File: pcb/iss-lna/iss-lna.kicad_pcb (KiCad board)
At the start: 2 copper layers, 65 x 32 mm, 46 parts, among them J1 SMA, J2 UFL, J3 UFL, J4 SMA, J5 UFL, J6 UFL, Q1 BFU520R

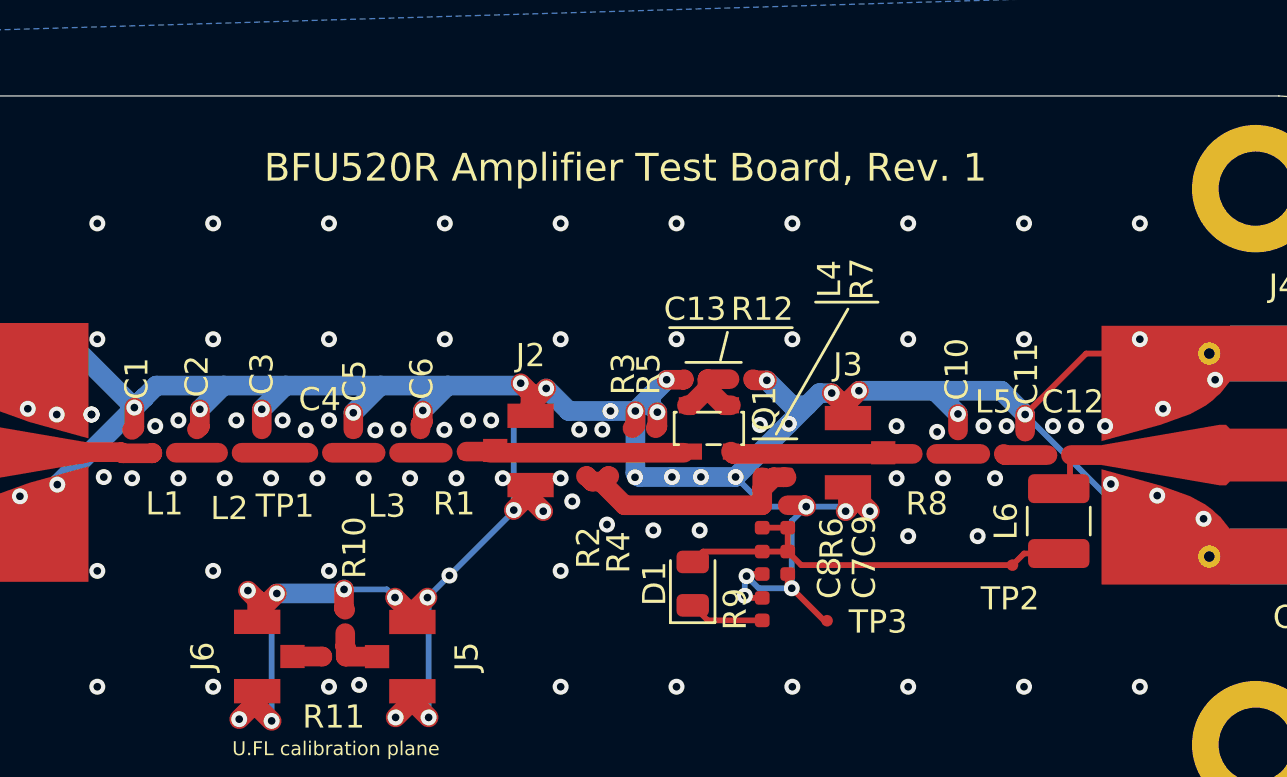
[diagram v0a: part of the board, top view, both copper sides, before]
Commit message: Fix component; base and collector are swapped!
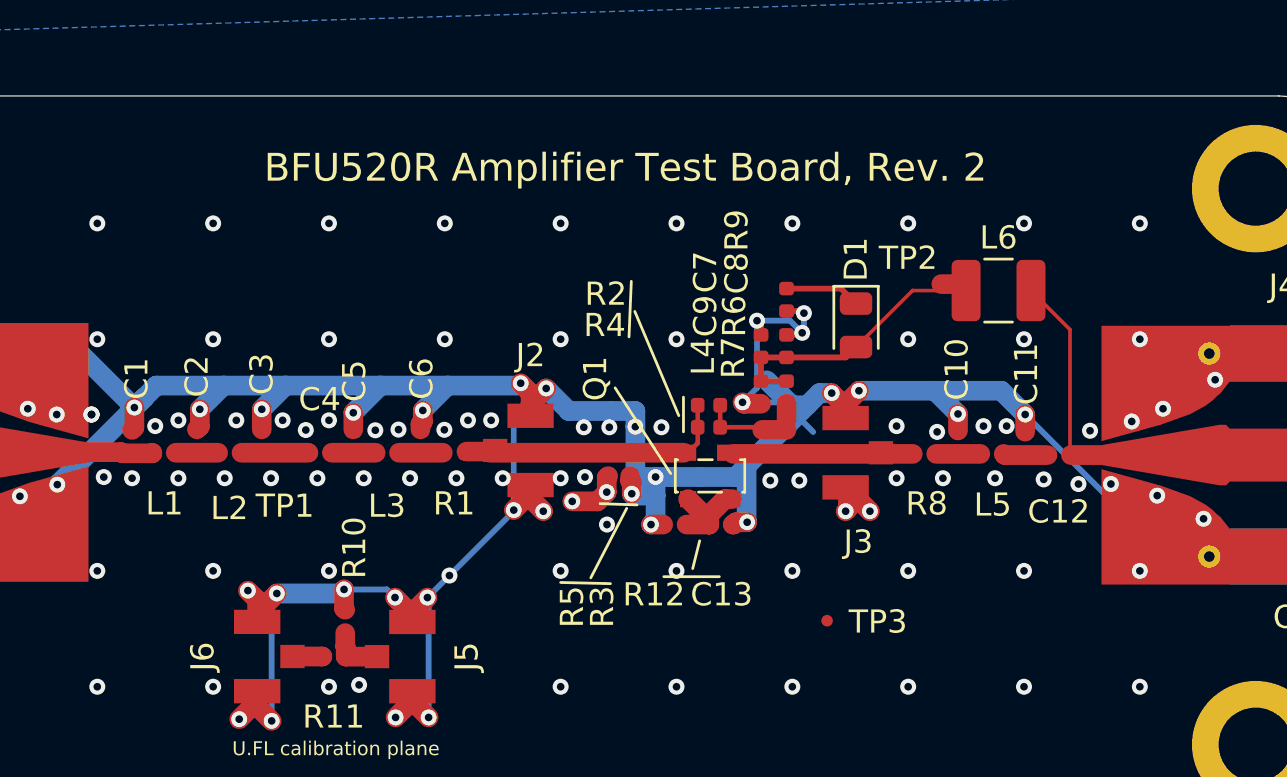
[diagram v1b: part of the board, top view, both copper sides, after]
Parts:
- moved R9 13.4 mm to (119.8, 50.8), turned to 270 degrees
- moved D1 13.2 mm to (122.8, 51.9), turned to 270 degrees
- moved TP2 12.5 mm to (126.4, 50.1)
- moved L6 10.3 mm to (128.9, 50.4), turned to 0 degrees
- moved C7 9.42 mm to (118.7, 52.8), turned to 90 degrees
- moved C8 9.41 mm to (119.8, 52.8), turned to 90 degrees
- moved R12 6.88 mm to (115.0, 60.5), turned to 180 degrees
- moved C13 6.36 mm to (116.9, 60.5), turned to 0 degrees
- moved R2 5.89 mm to (116.4, 55.4), turned to 180 degrees
- moved C9 5.47 mm to (118.7, 54.8), turned to 270 degrees
- moved R6 5.45 mm to (119.8, 54.8), turned to 270 degrees
- moved R4 4.58 mm to (116.4, 56.3), turned to 180 degrees
- moved R5 2.29 mm to (112.0, 57.9), turned to 270 degrees
- moved Q1 2.05 mm to (116.5, 58.4), turned to 180 degrees
- moved R3 1.03 mm to (113.0, 57.9), turned to 270 degrees
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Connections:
- Q1 pad 1: Net-(J2-Pad1) -> Net-(J3-Pad1)
- Q1 pad 2: Net-(J3-Pad1) -> Net-(J2-Pad1)
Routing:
- net Net-(L4-Pad1): track 11.0 -> 4.58 mm
- net Net-(C12-Pad2): track 12.3 -> 18.4 mm
- net /VCC: track 18.6 -> 13.4 mm
- net GND: track 178.9 -> 173.9 mm
- net Net-(J2-Pad1): track 9.61 -> 11.8 mm
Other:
- board text added: "BFU520R Amplifier Test Board, Rev. 2"
- board text removed: "BFU520R Amplifier Test Board, Rev. 1"
